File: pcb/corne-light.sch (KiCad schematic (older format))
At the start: 139 parts, among them J1 MJ-4PP-9, J2 OLED, J3 Conn_01x05, J6 MJ-4PP-9, J7 OLED, Q1 2N7002E, Q2 2N7002E, SW1 Rotary_Encoder_Switch, SW40 Rotary_Encoder_Switch, U1 ProMicro, U2 ProMicro

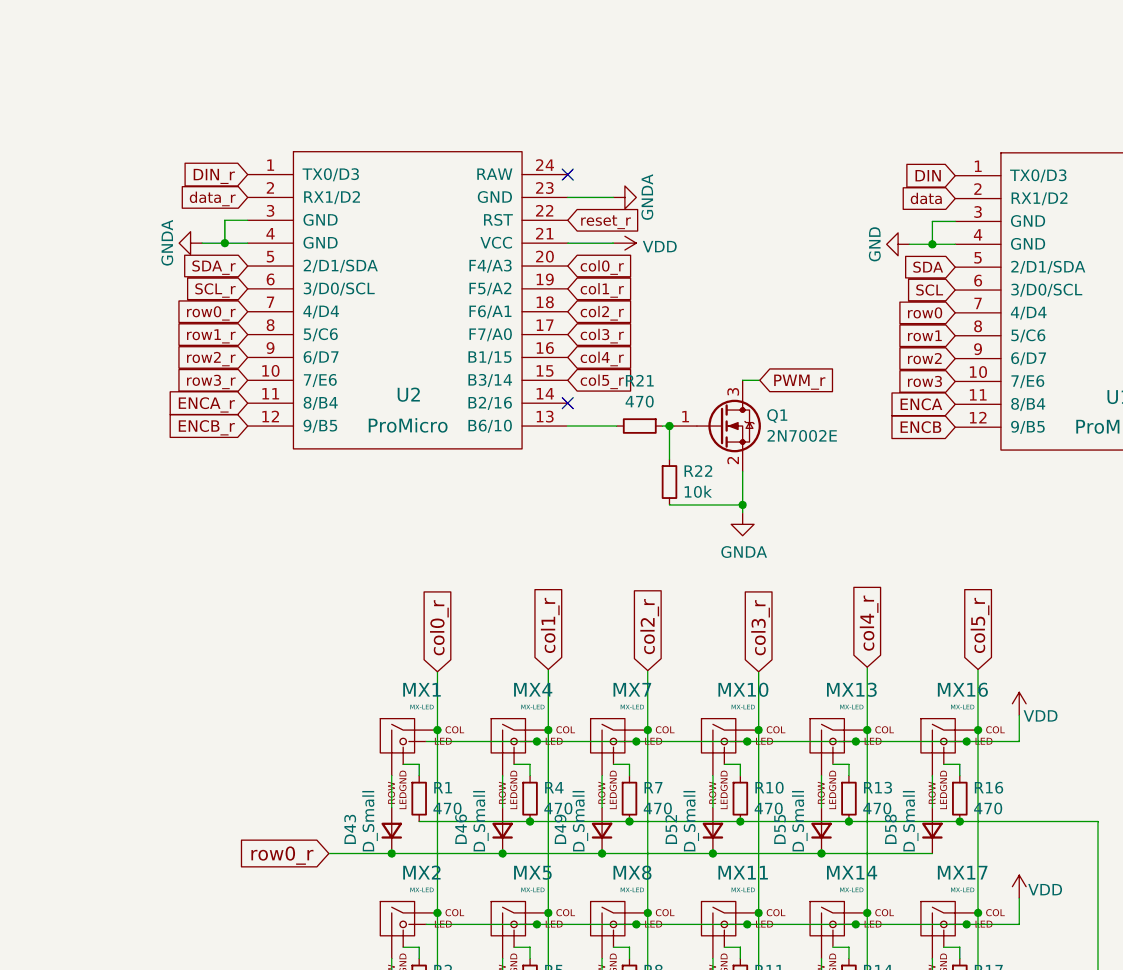
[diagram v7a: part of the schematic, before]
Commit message: Remove unecessary flag in schematic
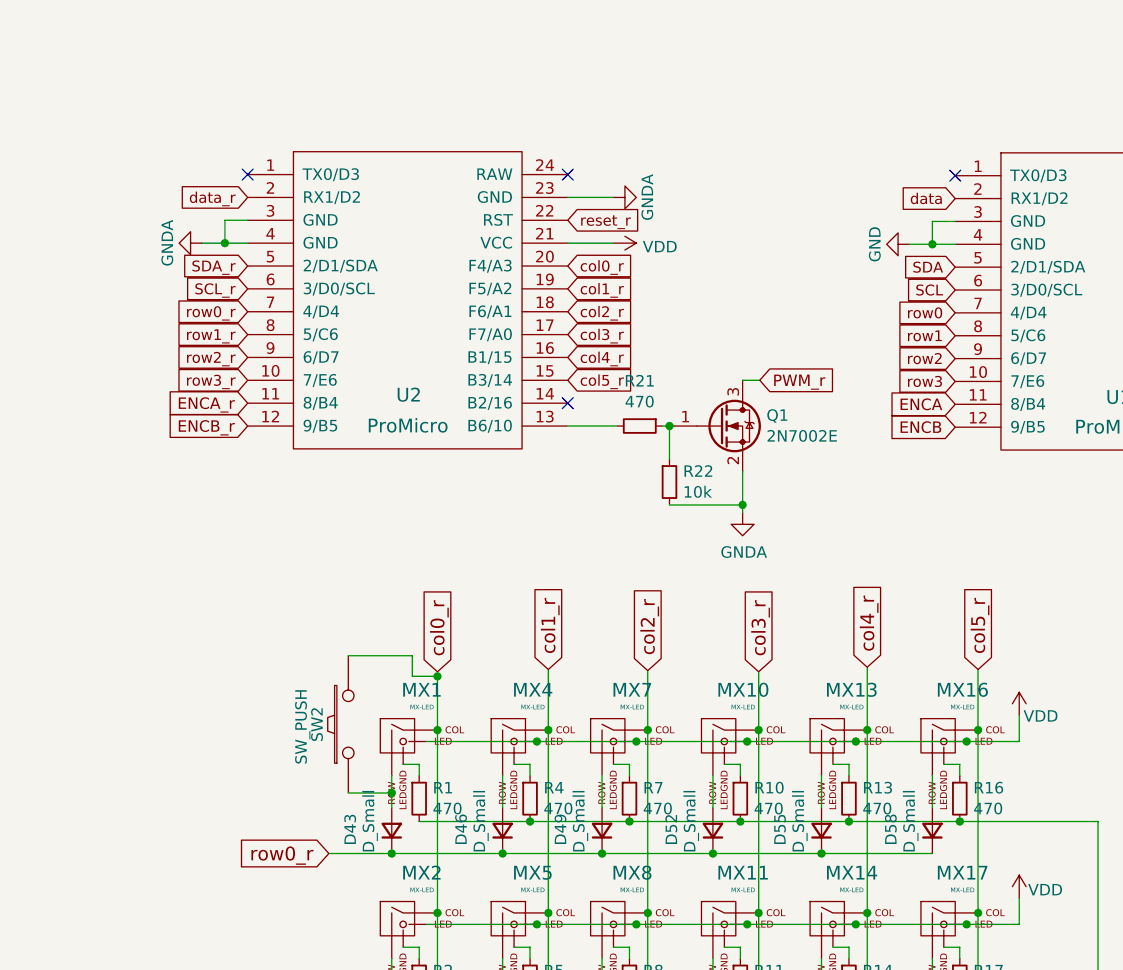
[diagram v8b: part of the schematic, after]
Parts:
- added SW2: SW_PUSH, MX_Alps_Hybrid:MX-1U, symbol kbd:SW_PUSH
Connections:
- net col0_r: now also SW2.2
- net at D43.2 (A), MX1.2 (ROW): now also SW2.1
- net DIN: no longer names the net of U1.1 (TX0/D3)
- net DIN_r: no longer names the net of U2.1 (TX0/D3)
- no-connect marks 9 -> 11
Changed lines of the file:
@@
 $EndComp
 Wire Wire Line
-	1680 3355 1680 3495
+	1680 3355 1680 3430
 $Comp
 L Device:D_Small D43
@@
 Text GLabel 1880 2900 1    60   Input ~ 0
 col0_r
-Wire Wire Line
-	1880 3155 1880 2900
 Connection ~ 1880 3155
 Wire Wire Line
@@
 Text GLabel 6385 1630 2    50   Input ~ 0
 PWM
-Text GLabel 1050 725  0    50   Input ~ 0
-DIN_r
-Text GLabel 4145 730  0    50   Input ~ 0
-DIN
 $Comp
 L Transistor_FET:2N7002E Q2
@@
 	1    0    0    -1
 $EndComp
+Wire Wire Line
+	1880 3155 1880 2920
+$Comp
+L kbd:SW_PUSH SW2
+U 1 1 60B688E8
+P 1490 3130
+F 0 "SW2" H 1490 3265 50  0000 C CNN
+F 1 "SW_PUSH" H 1480 3335 50  0000 C CNN
+F 2 "MX_Alps_Hybrid:MX-1U" H 1490 3130 50  0001 C CNN
+F 3 "" H 1490 3130 50  0000 C CNN
+	1    1490 3130
+	0    -1   -1   0
+$EndComp
+Wire Wire Line
+	1490 2830 1770 2830
+Wire Wire Line
+	1770 2830 1770 2920
+Wire Wire Line
+	1770 2920 1880 2920
+Connection ~ 1880 2920
+Wire Wire Line
+	1880 2920 1880 2900
+Wire Wire Line
+	1490 3430 1680 3430
+Connection ~ 1680 3430
+Wire Wire Line
+	1680 3430 1680 3495
+NoConn ~ 1050 725
+NoConn ~ 4145 730
 $EndSCHEMATC
